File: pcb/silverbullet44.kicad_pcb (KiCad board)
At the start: 2 copper layers, 155.6 x 105.4 mm, 94 parts, among them J1 Conn_01x04, J3 Conn_01x01, J4 Conn_01x01, J5 Conn_01x01, SW1 SW_PUSH, SW10 SW_PUSH, SW11 SW_PUSH, SW12 SW_PUSH, SW13 SW_PUSH, SW14 SW_PUSH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

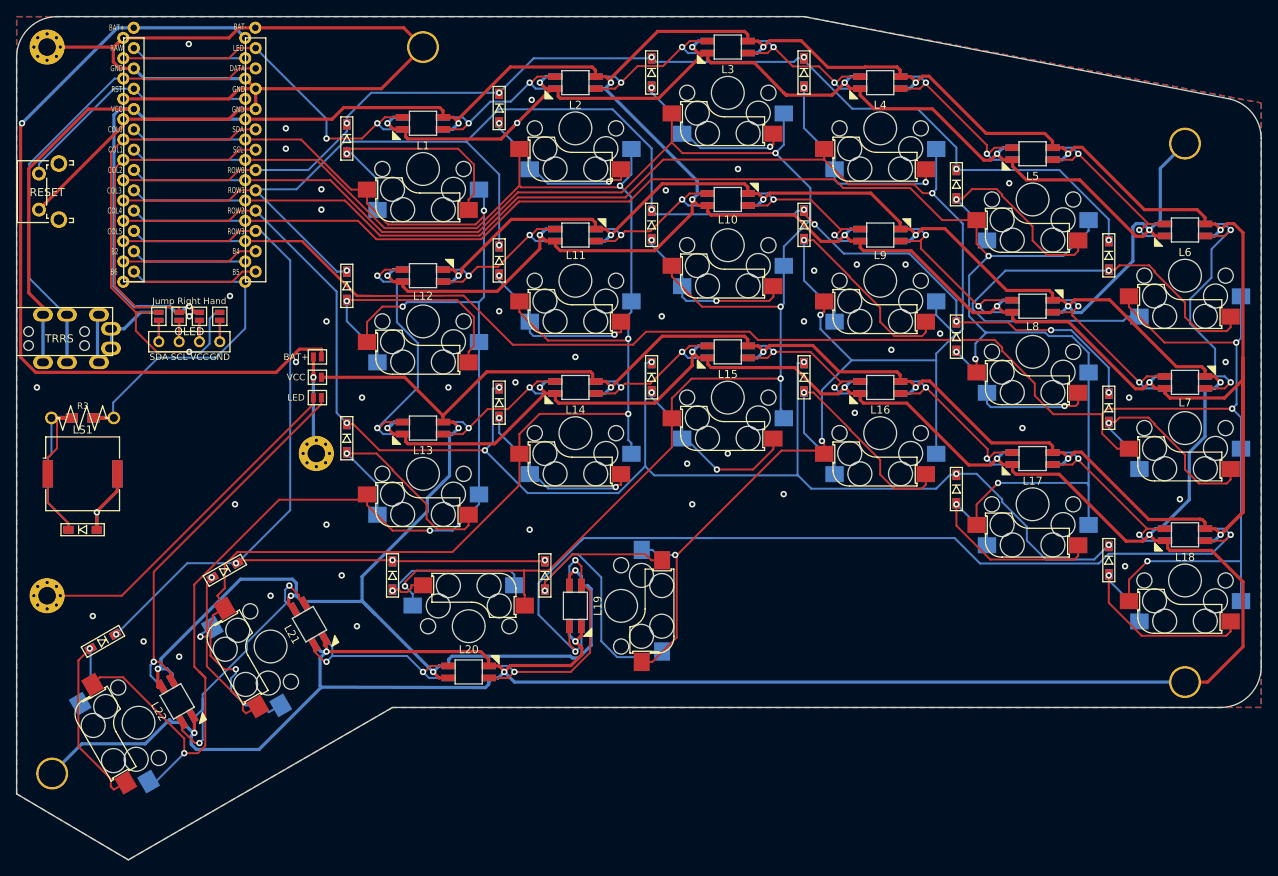
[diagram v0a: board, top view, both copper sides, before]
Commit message: add dwg dxf acrilcut data.
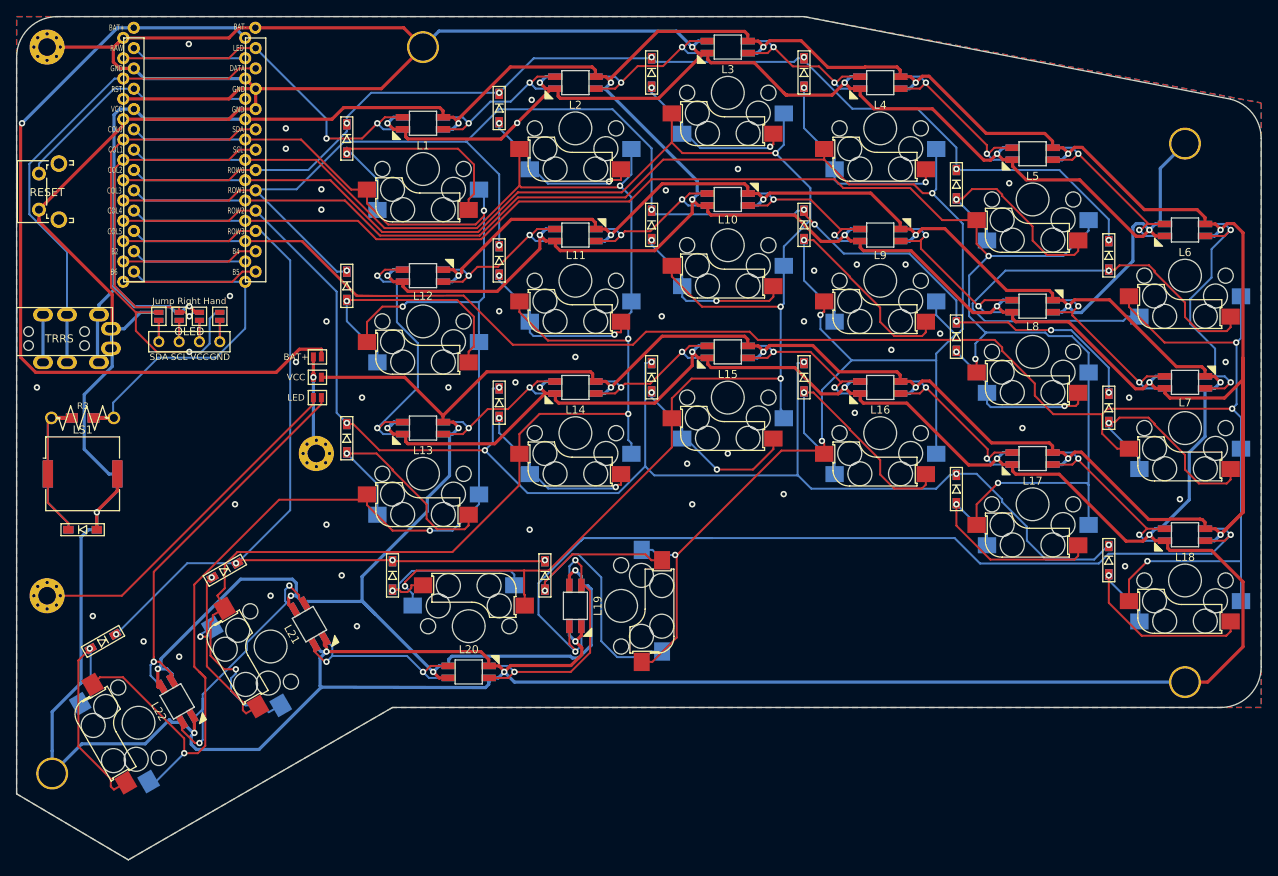
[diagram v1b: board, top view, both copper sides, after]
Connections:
- TRRS1 pad B: VCC -> Net-(TRRS1-PadB)
- TRRS1 pad D: Net-(TRRS1-PadD) -> VCC
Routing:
- net GND: track 859.2 -> 966.2 mm
- net VCC: track 756.3 -> 725.6 mm
- net Net-(TRRS1-PadD): track 6.11 -> 0.00 mm
- net Net-(TRRS1-PadB): track 0.00 -> 5.95 mm
- net Net-(D23-Pad1): track 35.8 -> 34.1 mm
